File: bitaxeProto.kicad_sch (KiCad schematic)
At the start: 10 parts, among them J1 XT30

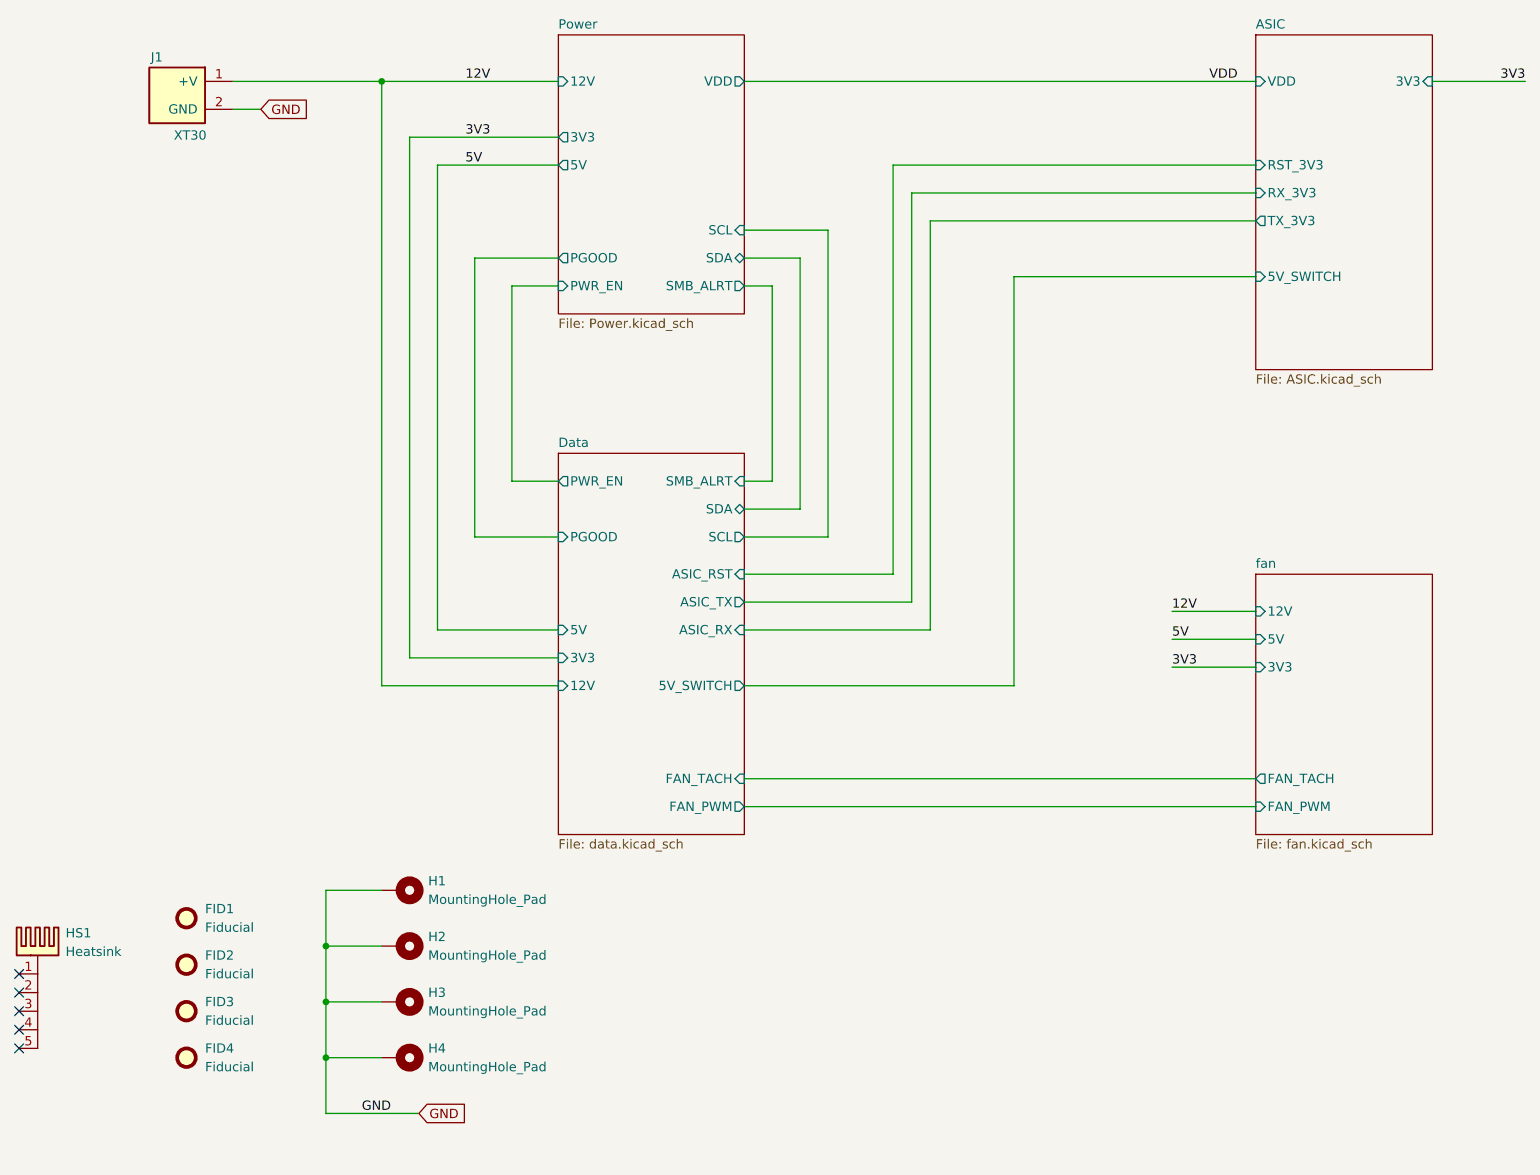
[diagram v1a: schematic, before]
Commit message: add domain voltage sensing for #3 -- just schematic so far
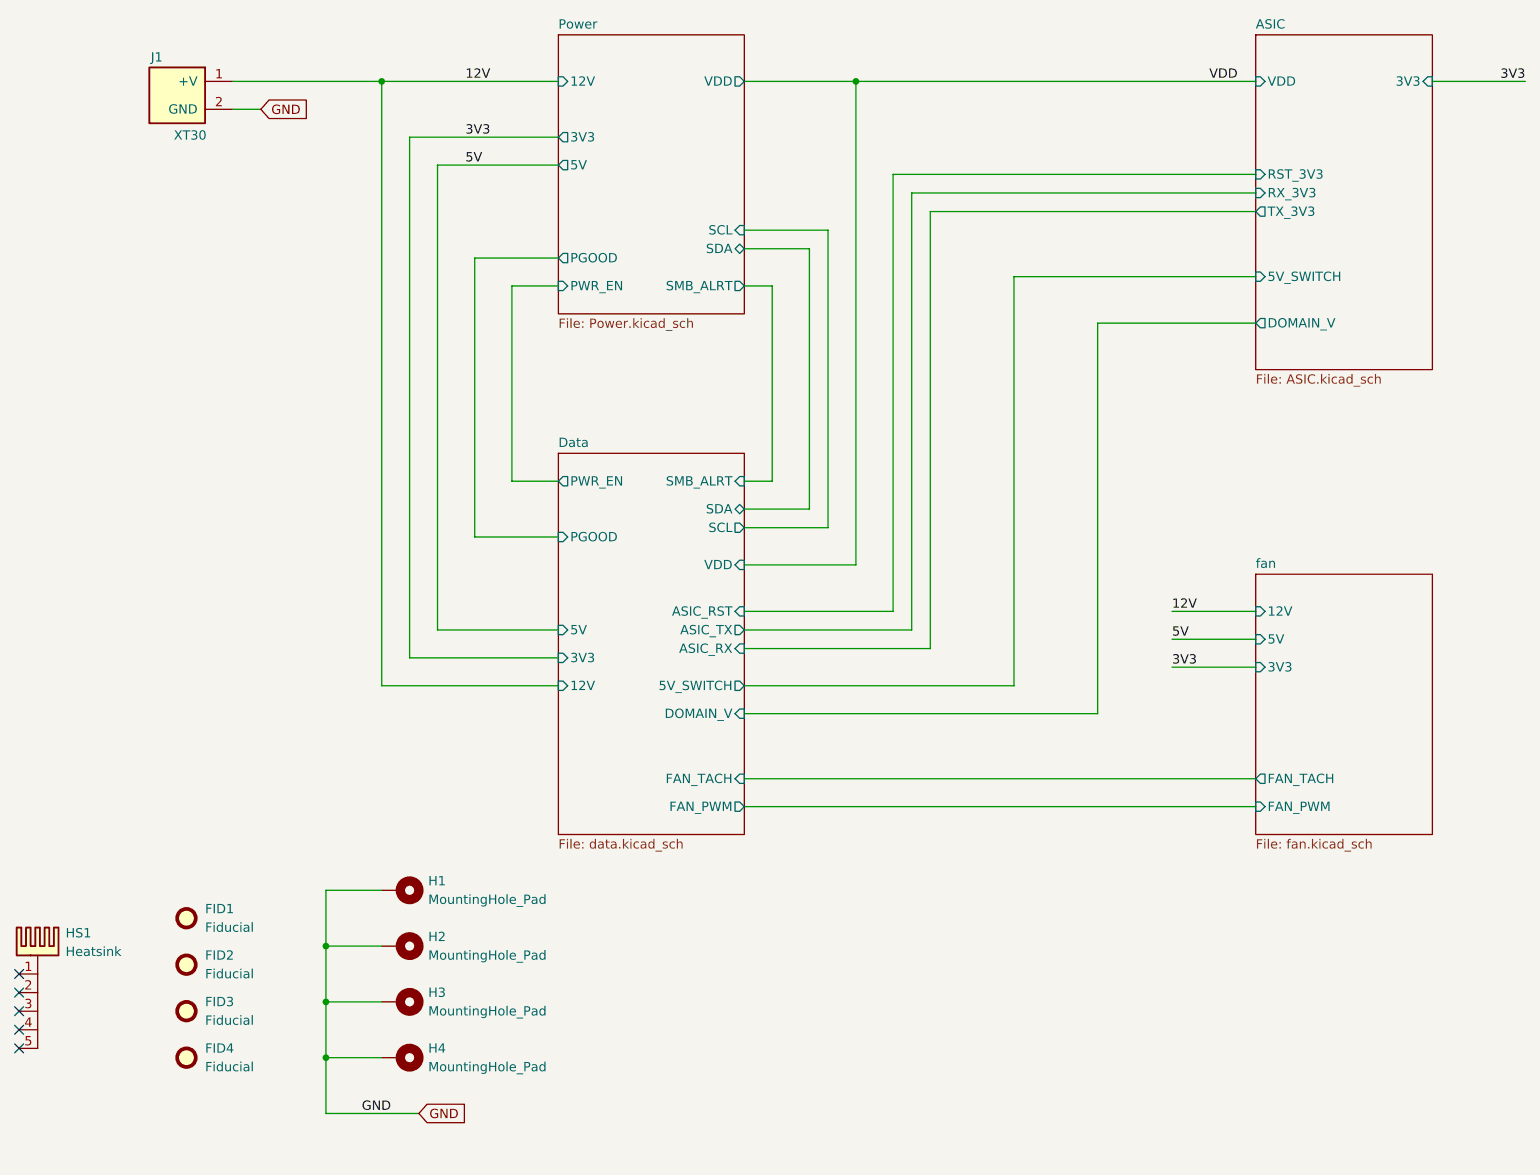
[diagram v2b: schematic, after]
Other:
- sheet ASIC ports: added DOMAIN_V; removed none
- sheet Data ports: added DOMAIN_V, VDD; removed none
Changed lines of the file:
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@@
+	)
+	(junction
+		(at 143.51 41.91)
+		(diameter 0)
+		(color 0 0 0 0)
 	)
 	(junction
@@
 	(wire
 		(pts
-			(xy 128.27 104.14) (xy 139.7 104.14)
+			(xy 128.27 102.87) (xy 139.7 102.87)
 		)
 		(stroke
@@
 	(wire
 		(pts
+			(xy 143.51 41.91) (xy 198.12 41.91)
+		)
+		(stroke
+			(width 0)
+			(type default)
+		)
+	)
+	(wire
+		(pts
+			(xy 176.53 74.93) (xy 198.12 74.93)
+		)
+		(stroke
+			(width 0)
+			(type default)
+		)
+	)
+	(wire
+		(pts
+			(xy 143.51 107.95) (xy 143.51 41.91)
+		)
+		(stroke
+			(width 0)
+			(type default)
+		)
+	)
+	(wire
+		(pts
 			(xy 71.12 160.02) (xy 78.74 160.02)
 		)
@@
 	(wire
 		(pts
-			(xy 153.67 116.84) (xy 128.27 116.84)
+			(xy 153.67 119.38) (xy 128.27 119.38)
 		)
 		(stroke
@@
 	(wire
 		(pts
-			(xy 151.13 57.15) (xy 151.13 113.03)
+			(xy 151.13 57.15) (xy 151.13 116.84)
 		)
 		(stroke
@@
 	(wire
 		(pts
-			(xy 135.89 66.04) (xy 135.89 100.33)
+			(xy 137.16 64.77) (xy 137.16 100.33)
 		)
 		(stroke
@@
 	(wire
 		(pts
+			(xy 128.27 107.95) (xy 143.51 107.95)
+		)
+		(stroke
+			(width 0)
+			(type default)
+		)
+	)
+	(wire
+		(pts
 			(xy 132.08 96.52) (xy 132.08 69.85)
 		)
@@
 	(wire
 		(pts
-			(xy 128.27 109.22) (xy 148.59 109.22)
+			(xy 128.27 114.3) (xy 148.59 114.3)
 		)
 		(stroke
@@
 	(wire
 		(pts
-			(xy 153.67 60.96) (xy 198.12 60.96)
+			(xy 153.67 59.69) (xy 198.12 59.69)
 		)
 		(stroke
@@
 	(wire
 		(pts
+			(xy 128.27 128.27) (xy 176.53 128.27)
+		)
+		(stroke
+			(width 0)
+			(type default)
+		)
+	)
+	(wire
+		(pts
 			(xy 82.55 120.65) (xy 82.55 49.53)
 		)
@@
 	(wire
 		(pts
-			(xy 153.67 60.96) (xy 153.67 116.84)
-		)
-		(stroke
-			(width 0)
-			(type default)
-		)
-	)
-	(wire
-		(pts
-			(xy 128.27 100.33) (xy 135.89 100.33)
+			(xy 153.67 59.69) (xy 153.67 119.38)
+		)
+		(stroke
+			(width 0)
+			(type default)
+		)
+	)
+	(wire
+		(pts
+			(xy 128.27 100.33) (xy 137.16 100.33)
 		)
 		(stroke
@@
 	(wire
 		(pts
+			(xy 176.53 128.27) (xy 176.53 74.93)
+		)
+		(stroke
+			(width 0)
+			(type default)
+		)
+	)
+	(wire
+		(pts
 			(xy 71.12 152.4) (xy 71.12 160.02)
 		)
@@
 	(wire
 		(pts
-			(xy 148.59 53.34) (xy 148.59 109.22)
-		)
-		(stroke
-			(width 0)
-			(type default)
-		)
-	)
-	(wire
-		(pts
-			(xy 128.27 41.91) (xy 198.12 41.91)
+			(xy 148.59 54.61) (xy 148.59 114.3)
+		)
+		(stroke
+			(width 0)
+			(type default)
+		)
+	)
+	(wire
+		(pts
+			(xy 128.27 41.91) (xy 143.51 41.91)
 		)
 		(stroke
@@
 	(wire
 		(pts
-			(xy 198.12 53.34) (xy 148.59 53.34)
+			(xy 198.12 54.61) (xy 148.59 54.61)
 		)
 		(stroke
@@
 	(wire
 		(pts
-			(xy 128.27 66.04) (xy 135.89 66.04)
+			(xy 128.27 64.77) (xy 137.16 64.77)
 		)
 		(stroke
@@
 	(wire
 		(pts
-			(xy 139.7 62.23) (xy 139.7 104.14)
-		)
-		(stroke
-			(width 0)
-			(type default)
-		)
-	)
-	(wire
-		(pts
-			(xy 151.13 113.03) (xy 128.27 113.03)
+			(xy 139.7 62.23) (xy 139.7 102.87)
+		)
+		(stroke
+			(width 0)
+			(type default)
+		)
+	)
+	(wire
+		(pts
+			(xy 151.13 116.84) (xy 128.27 116.84)
 		)
 		(stroke
@@
 		)
 		(pin "SCL" output
-			(at 128.27 104.14 0)
+			(at 128.27 102.87 0)
 			(effects
 				(font
@@
 		)
 		(pin "ASIC_RST" input
-			(at 128.27 109.22 0)
+			(at 128.27 114.3 0)
 			(effects
 				(font
@@
 		)
 		(pin "ASIC_RX" input
+			(at 128.27 119.38 0)
+			(effects
+				(font
+					(size 1.27 1.27)
+				)
+				(justify right)
+			)
+		)
+		(pin "ASIC_TX" output
 			(at 128.27 116.84 0)
 			(effects
@@
 			)
 		)
-		(pin "ASIC_TX" output
-			(at 128.27 113.03 0)
+		(pin "DOMAIN_V" input
+			(at 128.27 128.27 0)
+			(effects
+				(font
+					(size 1.27 1.27)
+				)
+				(justify right)
+			)
+		)
+		(pin "VDD" input
+			(at 128.27 107.95 0)
 			(effects
 				(font
@@
 		)
 		(pin "SDA" bidirectional
-			(at 128.27 66.04 0)
+			(at 128.27 64.77 0)
 			(effects
 				(font
@@
 		)
 		(pin "RST_3V3" input
-			(at 198.12 53.34 180)
+			(at 198.12 54.61 180)
 			(effects
 				(font
@@
 		)
 		(pin "TX_3V3" output
-			(at 198.12 60.96 180)
-			(effects
-				(font
+			(at 198.12 59.69 180)
+			(effects
+				(font
+					(size 1.27 1.27)
+				)
+				(justify left)
+			)
+		)
+		(pin "DOMAIN_V" output
+			(at 198.12 74.93 180)
+			(effects
+				(font

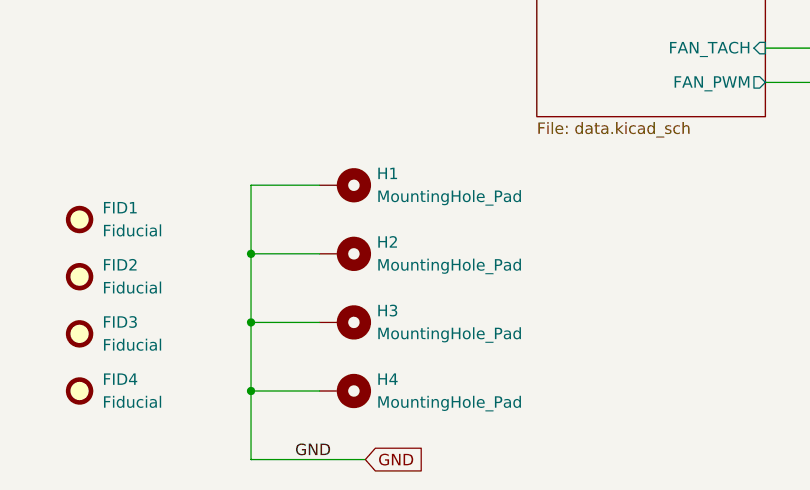
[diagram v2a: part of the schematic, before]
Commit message: new smaller board outline. repositioned a lot of components
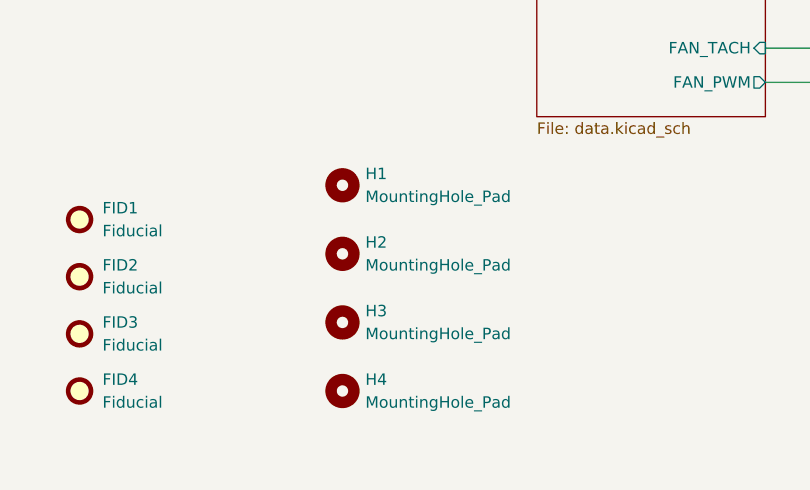
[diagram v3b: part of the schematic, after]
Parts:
- H1, H2, H3, H4: footprint MountingHole:MountingHole_3.2mm_M3_Pad_Via -> MountingHole:MountingHole_3.2mm_M3; symbol Mechanical:MountingHole_Pad -> Mechanical:MountingHole
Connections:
- net GND: no longer H1.1, H2.1, H3.1, H4.1
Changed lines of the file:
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@@
-	)
-	(junction
-		(at 71.12 160.02)
-		(diameter 0)
-		(color 0 0 0 0)
-	)
-	(junction
-		(at 71.12 175.26)
-		(diameter 0)
-		(color 0 0 0 0)
 	)
 	(junction
@@
 		(color 0 0 0 0)
 	)
-	(junction
-		(at 71.12 167.64)
-		(diameter 0)
-		(color 0 0 0 0)
-	)
 	(no_connect
 		(at 29.21 171.45)
@@
 	(wire
 		(pts
-			(xy 71.12 160.02) (xy 78.74 160.02)
-		)
-		(stroke
-			(width 0)
-			(type default)
-		)
-	)
-	(wire
-		(pts
 			(xy 153.67 119.38) (xy 128.27 119.38)
 		)
@@
 	(wire
 		(pts
-			(xy 71.12 175.26) (xy 71.12 182.88)
-		)
-		(stroke
-			(width 0)
-			(type default)
-		)
-	)
-	(wire
-		(pts
-			(xy 78.74 152.4) (xy 71.12 152.4)
-		)
-		(stroke
-			(width 0)
-			(type default)
-		)
-	)
-	(wire
-		(pts
 			(xy 151.13 57.15) (xy 151.13 116.84)
 		)
@@
 	(wire
 		(pts
-			(xy 71.12 182.88) (xy 83.82 182.88)
-		)
-		(stroke
-			(width 0)
-			(type default)
-		)
-	)
-	(wire
-		(pts
 			(xy 91.44 66.04) (xy 91.44 104.14)
 		)
@@
 	(wire
 		(pts
-			(xy 71.12 175.26) (xy 78.74 175.26)
-		)
-		(stroke
-			(width 0)
-			(type default)
-		)
-	)
-	(wire
-		(pts
 			(xy 96.52 69.85) (xy 96.52 96.52)
 		)
@@
 	(wire
 		(pts
-			(xy 71.12 152.4) (xy 71.12 160.02)
-		)
-		(stroke
-			(width 0)
-			(type default)
-		)
-	)
-	(wire
-		(pts
 			(xy 148.59 54.61) (xy 148.59 114.3)
 		)
@@
 	(wire
 		(pts
-			(xy 71.12 160.02) (xy 71.12 167.64)
-		)
-		(stroke
-			(width 0)
-			(type default)
-		)
-	)
-	(wire
-		(pts
 			(xy 102.87 69.85) (xy 96.52 69.85)
 		)
@@
 	(wire
 		(pts
-			(xy 71.12 167.64) (xy 71.12 175.26)
-		)
-		(stroke
-			(width 0)
-			(type default)
-		)
-	)
-	(wire
-		(pts
 			(xy 102.87 124.46) (xy 78.74 124.46)
 		)
@@
 		(pts
 			(xy 78.74 41.91) (xy 78.74 124.46)
-		)
-		(stroke
-			(width 0)
-			(type default)
-		)
-	)
-	(wire
-		(pts
-			(xy 71.12 167.64) (xy 78.74 167.64)
 		)
 		(stroke
@@
 		)
 	)
-	(label "GND"
-		(at 80.01 182.88 180)
-		(effects
-			(font
-				(size 1.27 1.27)
-			)
-			(justify right bottom)
-		)
-	)
 	(label "3V3"
 		(at 186.69 121.92 0)
@@
 			)
 			(justify left bottom)
-		)
-	)
-	(global_label "GND"
-		(shape input)
-		(at 83.82 182.88 0)
-		(fields_autoplaced yes)
-		(effects
-			(font
-				(size 1.27 1.27)
-			)
-			(justify left)
-		)
-		(property "Intersheetrefs" "${INTERSHEET_REFS}"
-			(at 90.6757 182.88 0)
-			(hide yes)
-			(show_name no)
-			(do_not_autoplace no)
-			(effects
-				(font
-					(size 1.27 1.27)
-				)
-				(justify left)
-			)
 		)
 	)
@@
 	)
 	(symbol
-		(lib_id "Mechanical:MountingHole_Pad")
+		(lib_id "Mechanical:MountingHole")
 		(at 81.28 160.02 270)
 		(unit 1)
@@
 		(fields_autoplaced yes)
 		(property "Reference" "H2"
-			(at 85.09 158.7499 90)
+			(at 83.82 158.7499 90)
 			(show_name no)
 			(do_not_autoplace no)
@@
 		)
 		(property "Value" "MountingHole_Pad"
-			(at 85.09 161.2899 90)
+			(at 83.82 161.2899 90)
 			(show_name no)
 			(do_not_autoplace no)
@@
 			)
 		)
-		(property "Footprint" "MountingHole:MountingHole_3.2mm_M3_Pad_Via"
+		(property "Footprint" "MountingHole:MountingHole_3.2mm_M3"
 			(at 81.28 160.02 0)
 			(hide yes)
@@
 			)
 		)
-		(property "Description" "Mounting Hole with connection"
+		(property "Description" "Mounting Hole without connection"
 			(at 81.28 160.02 0)
 			(hide yes)
@@
 				)
 			)
-		)
-		(pin "1"
 		)
 		(instances
@@
 	)
 	(symbol
-		(lib_id "Mechanical:MountingHole_Pad")
+		(lib_id "Mechanical:MountingHole")
 		(at 81.28 175.26 270)
 		(unit 1)
 		(body_style 1)
-		(exclude_from_sim yes)
+		(exclude_from_sim no)
 		(in_bom no)
 		(on_board yes)
@@
 		(fields_autoplaced yes)
 		(property "Reference" "H4"
-			(at 85.09 173.9899 90)
+			(at 83.82 173.9899 90)
 			(show_name no)
 			(do_not_autoplace no)
@@
 		)
 		(property "Value" "MountingHole_Pad"
-			(at 85.09 176.5299 90)
+			(at 83.82 176.5299 90)
 			(show_name no)
 			(do_not_autoplace no)
@@
 			)
 		)
-		(property "Footprint" "MountingHole:MountingHole_3.2mm_M3_Pad_Via"
+		(property "Footprint" "MountingHole:MountingHole_3.2mm_M3"
 			(at 81.28 175.26 0)
 			(hide yes)
@@
 			)
 		)
-		(property "Description" "Mounting Hole with connection"
+		(property "Description" "Mounting Hole without connection"
 			(at 81.28 175.26 0)
 			(hide yes)
@@
 				)
 			)
-		)
-		(pin "1"
 		)
 		(instances
@@
 	)
 	(symbol
-		(lib_id "Mechanical:MountingHole_Pad")
+		(lib_id "Mechanical:MountingHole")
 		(at 81.28 167.64 270)
 		(unit 1)
 		(body_style 1)
-		(exclude_from_sim yes)
+		(exclude_from_sim no)
 		(in_bom no)
 		(on_board yes)
@@
 		(fields_autoplaced yes)
 		(property "Reference" "H3"
-			(at 85.09 166.3699 90)
+			(at 83.82 166.3699 90)
 			(show_name no)
 			(do_not_autoplace no)
@@
 		)
 		(property "Value" "MountingHole_Pad"
-			(at 85.09 168.9099 90)
+			(at 83.82 168.9099 90)
 			(show_name no)
 			(do_not_autoplace no)
@@
 			)
 		)
-		(property "Footprint" "MountingHole:MountingHole_3.2mm_M3_Pad_Via"
+		(property "Footprint" "MountingHole:MountingHole_3.2mm_M3"
 			(at 81.28 167.64 0)
 			(hide yes)
@@
 			)
 		)
-		(property "Description" "Mounting Hole with connection"
+		(property "Description" "Mounting Hole without connection"
 			(at 81.28 167.64 0)
 			(hide yes)
@@
 				)
 			)
-		)
-		(pin "1"
 		)
 		(instances
@@
 	)
 	(symbol
-		(lib_id "Mechanical:MountingHole_Pad")
+		(lib_id "Mechanical:MountingHole")
 		(at 81.28 152.4 270)
 		(unit 1)
@@
 		(fields_autoplaced yes)
 		(property "Reference" "H1"
-			(at 85.09 151.1299 90)
+			(at 83.82 151.1299 90)
 			(show_name no)
 			(do_not_autoplace no)
@@
 		)
 		(property "Value" "MountingHole_Pad"
-			(at 85.09 153.6699 90)
+			(at 83.82 153.6699 90)
 			(show_name no)
 			(do_not_autoplace no)
@@
 			)
 		)
-		(property "Footprint" "MountingHole:MountingHole_3.2mm_M3_Pad_Via"
+		(property "Footprint" "MountingHole:MountingHole_3.2mm_M3"
 			(at 81.28 152.4 0)
 			(hide yes)
@@
 			)
 		)
-		(property "Description" "Mounting Hole with connection"
+		(property "Description" "Mounting Hole without connection"
 			(at 81.28 152.4 0)
 			(hide yes)
@@
 			)
 		)
-		(pin "1"
-		)
 		(instances

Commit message: changed fan connector footprint back to normal. lots of part substitutions for JLCPCB. Mounting hole changes for enclosure
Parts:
- added H5, H6, H7, H8: MountingHole_Pad, bitaxe:MountingHole_3.2mm_M3, symbol Mechanical:MountingHole
- H1, H2, H3, H4: footprint MountingHole:MountingHole_3.2mm_M3 -> bitaxe:MountingHole_3.2mm_M3
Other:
- note added: "Case Mounts"
- note added: "PCB Mounts"
- moved on the sheet: H1, H2, H3, H4

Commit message: switch to cheaper USB-C connector
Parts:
- J1: PARTNO XT30PW-M -> XT30PW-M30.G.Y
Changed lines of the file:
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@@
 			)
 		)
-		(property "PARTNO" "XT30PW-M"
+		(property "PARTNO" "XT30PW-M30.G.Y"
 			(at 50.546 56.642 0)
 			(hide yes)

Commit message: updated part attributes for JLCPCB Fabrication Toolkit
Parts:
- J1: FT Origin (none) -> Center; FT Rotation Offset (none) -> 180
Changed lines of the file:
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@@
+			)
+		)
+		(property "FT Origin" "Center"
+			(at 50.8 43.18 0)
+			(hide yes)
+			(show_name no)
+			(do_not_autoplace no)
+			(effects
+				(font
+					(size 1.27 1.27)
+				)
+			)
+		)
+		(property "FT Rotation Offset" "180"
+			(at 50.8 43.18 0)
+			(hide yes)
+			(show_name no)
+			(do_not_autoplace no)
+			(effects
+				(font
+					(size 1.27 1.27)
+				)
 			)
 		)
